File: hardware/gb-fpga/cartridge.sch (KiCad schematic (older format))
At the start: 4 parts, among them J2 Cartridge-32pin, U6 NVT2010, U7 NVT2010, U8 NVT2010

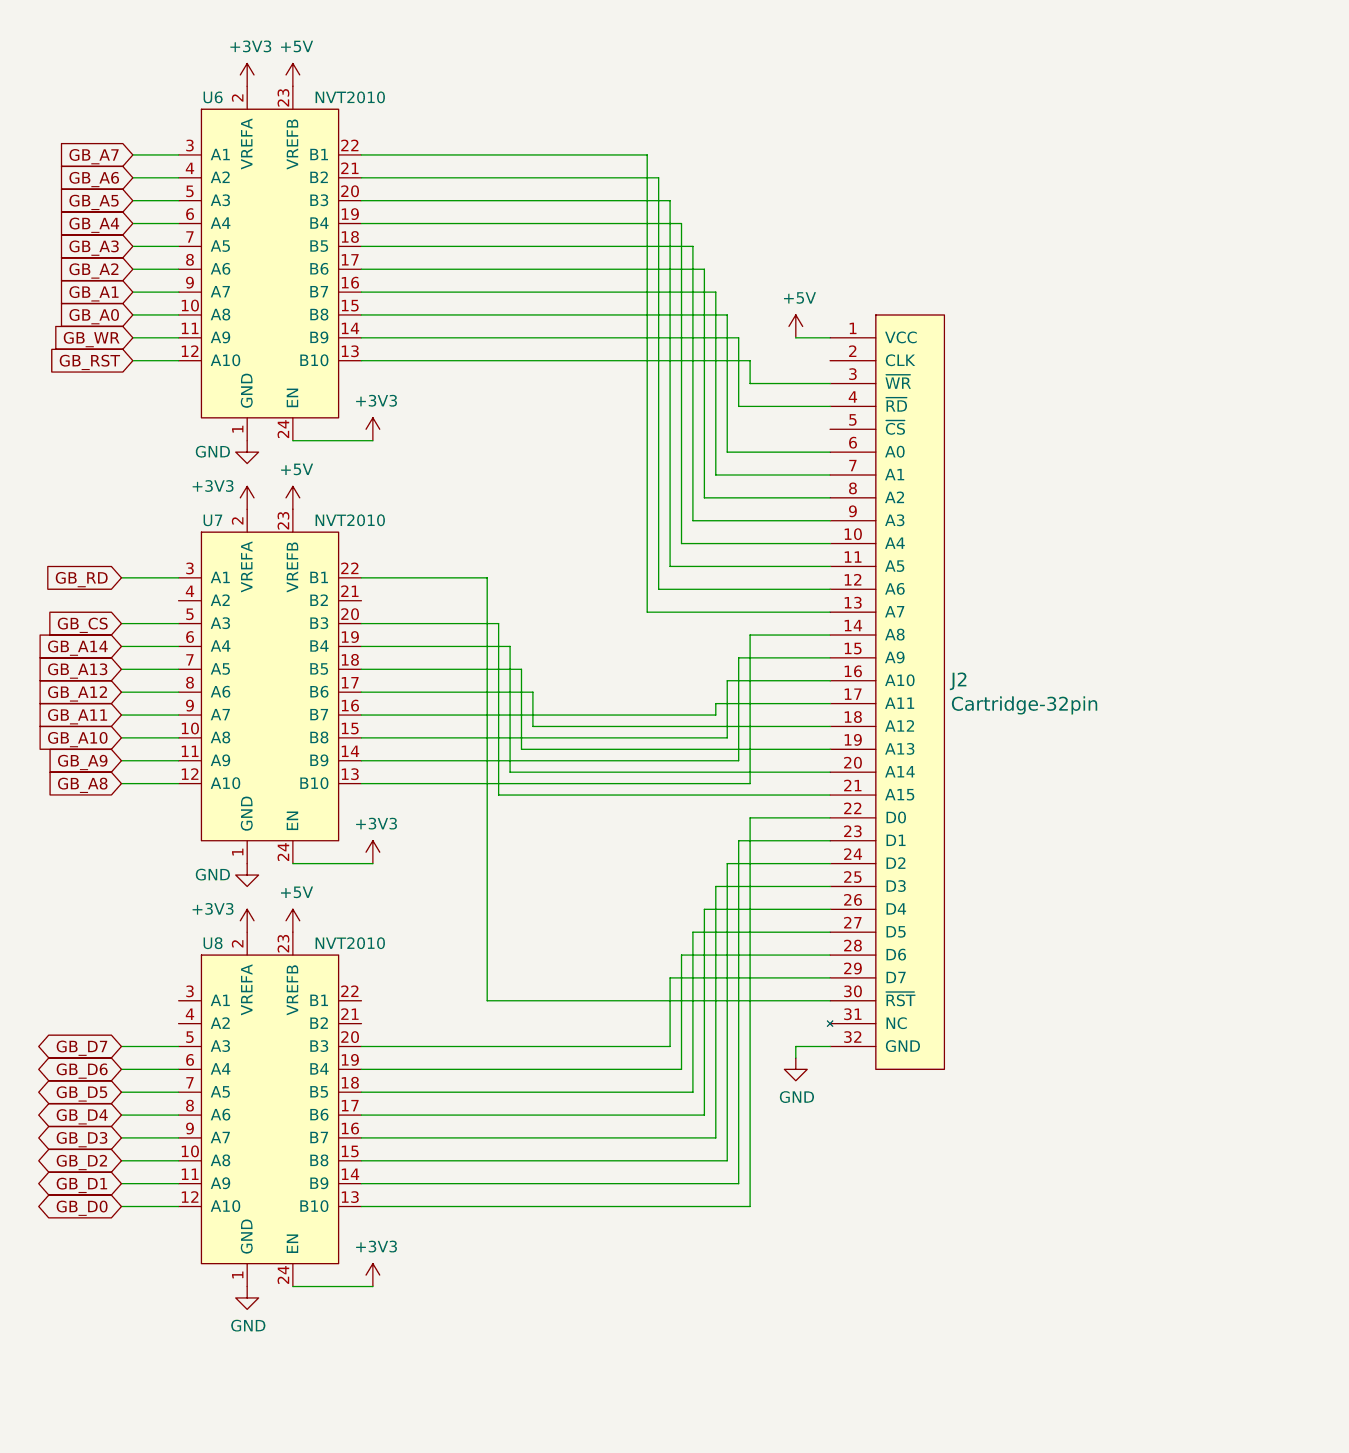
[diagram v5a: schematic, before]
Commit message: Fix cartridge pin out and replace voltage translators
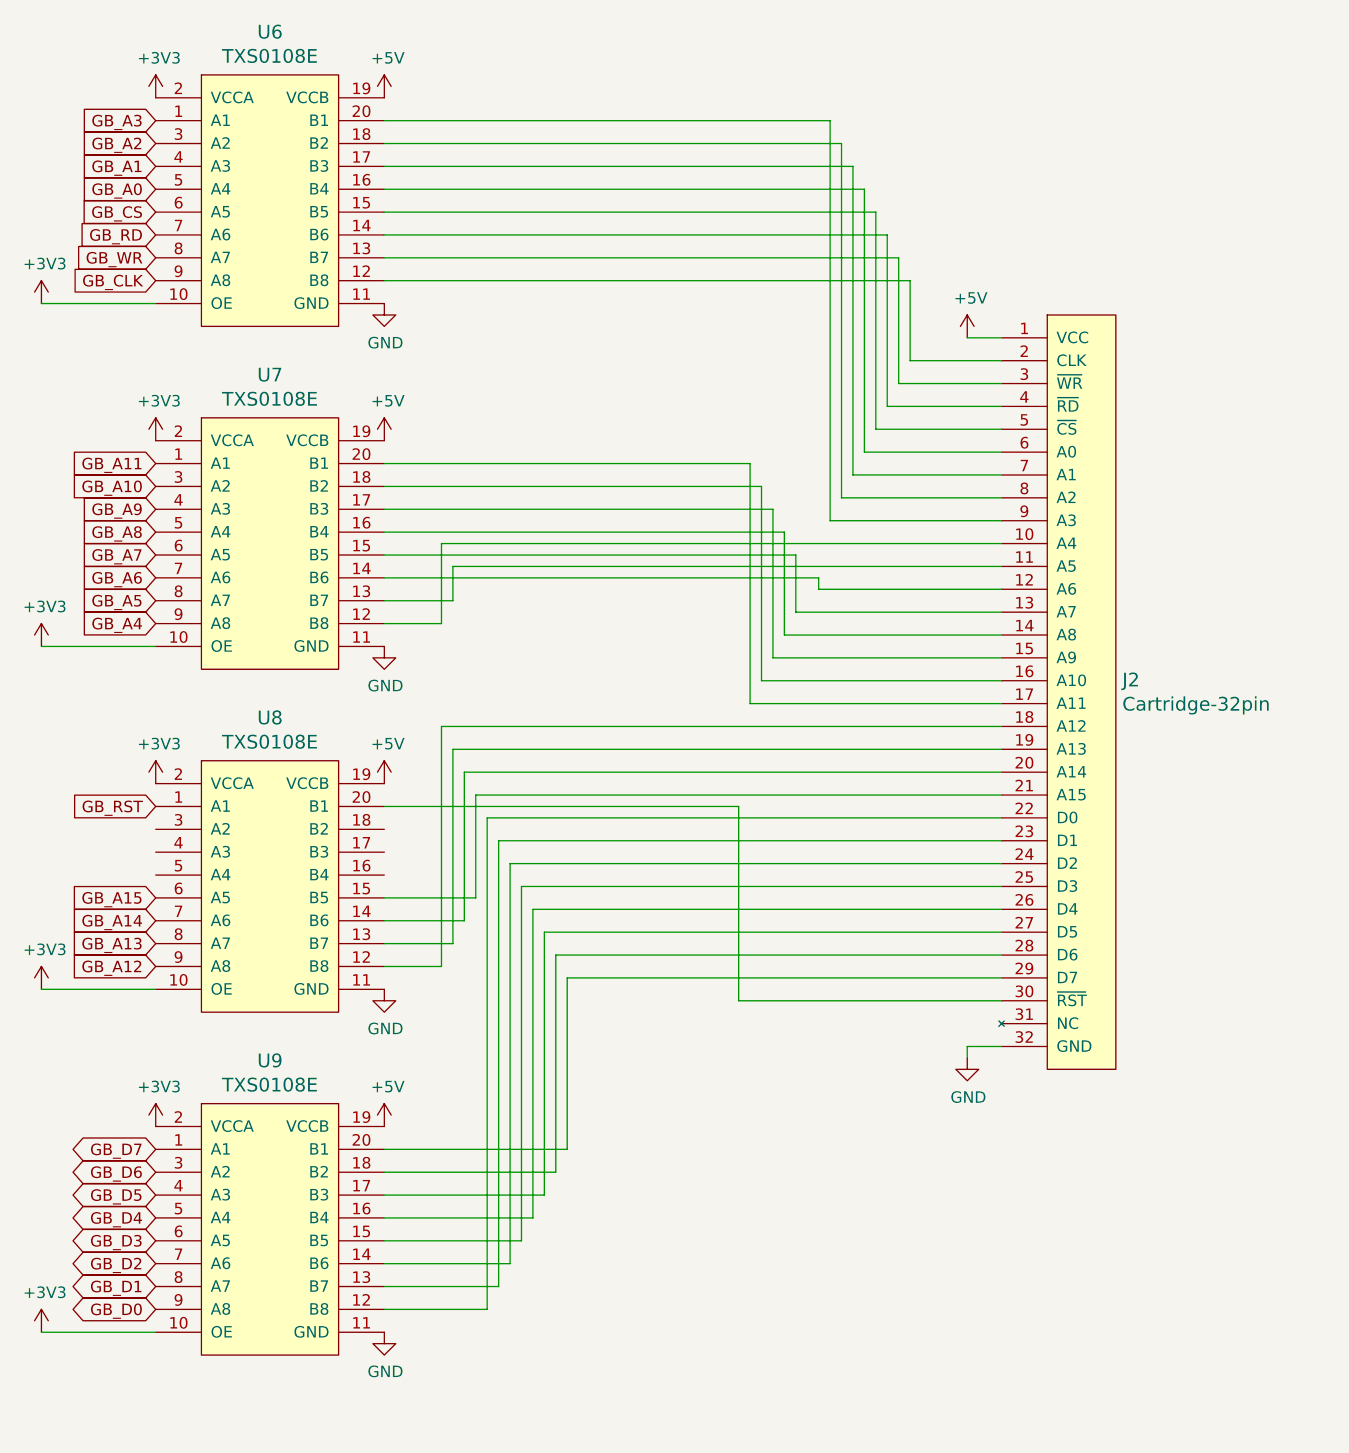
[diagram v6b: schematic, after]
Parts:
- removed U6, U7, U8: NVT2010, Package_SO:TSSOP-24_4.4x7.8mm_P0.65mm, symbol Logic_LevelTranslator:NVT2010
- added U6, U7, U8, U9: TXS0108E, Package_SO:TSSOP-20_4.4x6.5mm_P0.65mm, symbol gb-fpga:TXS0108E
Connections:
- net +3V3: now also U6.10 (OE), U6.2 (VCCA), U7.10 (OE), U7.2 (VCCA), U8.10 (OE), U8.2 (VCCA), U9.10 (OE), U9.2 (VCCA)
- net +5V: now also U6.19 (VCCB), U7.19 (VCCB), U8.19 (VCCB), U9.19 (VCCB)
- net GB_A0: now also U6.5 (A4)
- net GB_A1: now also U6.4 (A3)
- net GB_A10: now also U7.3 (A2)
- net GB_A11: now also U7.1 (A1)
- net GB_A12: now also U8.9 (A8)
- net GB_A13: now also U8.8 (A7)
- net GB_A14: now also U8.7 (A6)
- net GB_A2: now also U6.3 (A2)
- net GB_A3: now also U6.1 (A1)
- net GB_A4: now also U7.9 (A8)
- net GB_A5: now also U7.8 (A7)
- net GB_A6: now also U7.7 (A6)
- net GB_A7: now also U7.6 (A5)
- net GB_A8: now also U7.5 (A4)
- net GB_A9: now also U7.4 (A3)
- net GB_CS: now also U6.6 (A5)
- net GB_D0: now also U9.9 (A8)
- net GB_D1: now also U9.8 (A7)
- net GB_D2: now also U9.7 (A6)
- net GB_D3: now also U9.6 (A5)
- net GB_D4: now also U9.5 (A4)
- net GB_D5: now also U9.4 (A3)
- net GB_D6: now also U9.3 (A2)
- net GB_D7: now also U9.1 (A1)
- net GB_RD: now also U6.7 (A6)
- net GB_RST: now also U8.1 (A1)
- net GB_WR: now also U6.8 (A7)
- net GND: now also U6.11 (GND), U7.11 (GND), U8.11 (GND), U9.11 (GND)
- net at J2.10 (A4): now also U7.12 (B8)
- net at J2.11 (A5): now also U7.13 (B7)
- net at J2.12 (A6): now also U7.14 (B6)
- net at J2.13 (A7): now also U7.15 (B5)
- net at J2.14 (A8): now also U7.16 (B4)
- net at J2.15 (A9): now also U7.17 (B3)
- net at J2.16 (A10): now also U7.18 (B2)
- net at J2.17 (A11): now also U7.20 (B1)
- net at J2.18 (A12): now also U8.12 (B8)
- net at J2.19 (A13): now also U8.13 (B7)
- net at J2.2 (CLK): now also U6.12 (B8)
- net at J2.20 (A14): now also U8.14 (B6)
- net at J2.21 (A15): now also U8.15 (B5)
- net at J2.22 (D0): now also U9.12 (B8)
- net at J2.23 (D1): now also U9.13 (B7)
- net at J2.24 (D2): now also U9.14 (B6)
- net at J2.25 (D3): now also U9.15 (B5)
- net at J2.26 (D4): now also U9.16 (B4)
- net at J2.27 (D5): now also U9.17 (B3)
- net at J2.28 (D6): now also U9.18 (B2)
- net at J2.29 (D7): now also U9.20 (B1)
- net at J2.3 (~WR~): now also U6.13 (B7)
- net at J2.30 (~RST~): now also U8.20 (B1)
- net at J2.4 (~RD~): now also U6.14 (B6)
- net at J2.5 (~CS~): now also U6.15 (B5)
- net at J2.6 (A0): now also U6.16 (B4)
- net at J2.7 (A1): now also U6.17 (B3)
- net at J2.8 (A2): now also U6.18 (B2)
- net at J2.9 (A3): now also U6.20 (B1)
- new net GB_A15: U8.6 (A5)
- new net GB_CLK: U6.9 (A8)
